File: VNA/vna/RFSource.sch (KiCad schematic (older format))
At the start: 15 parts, among them U4 AD9851, X1 30MHz

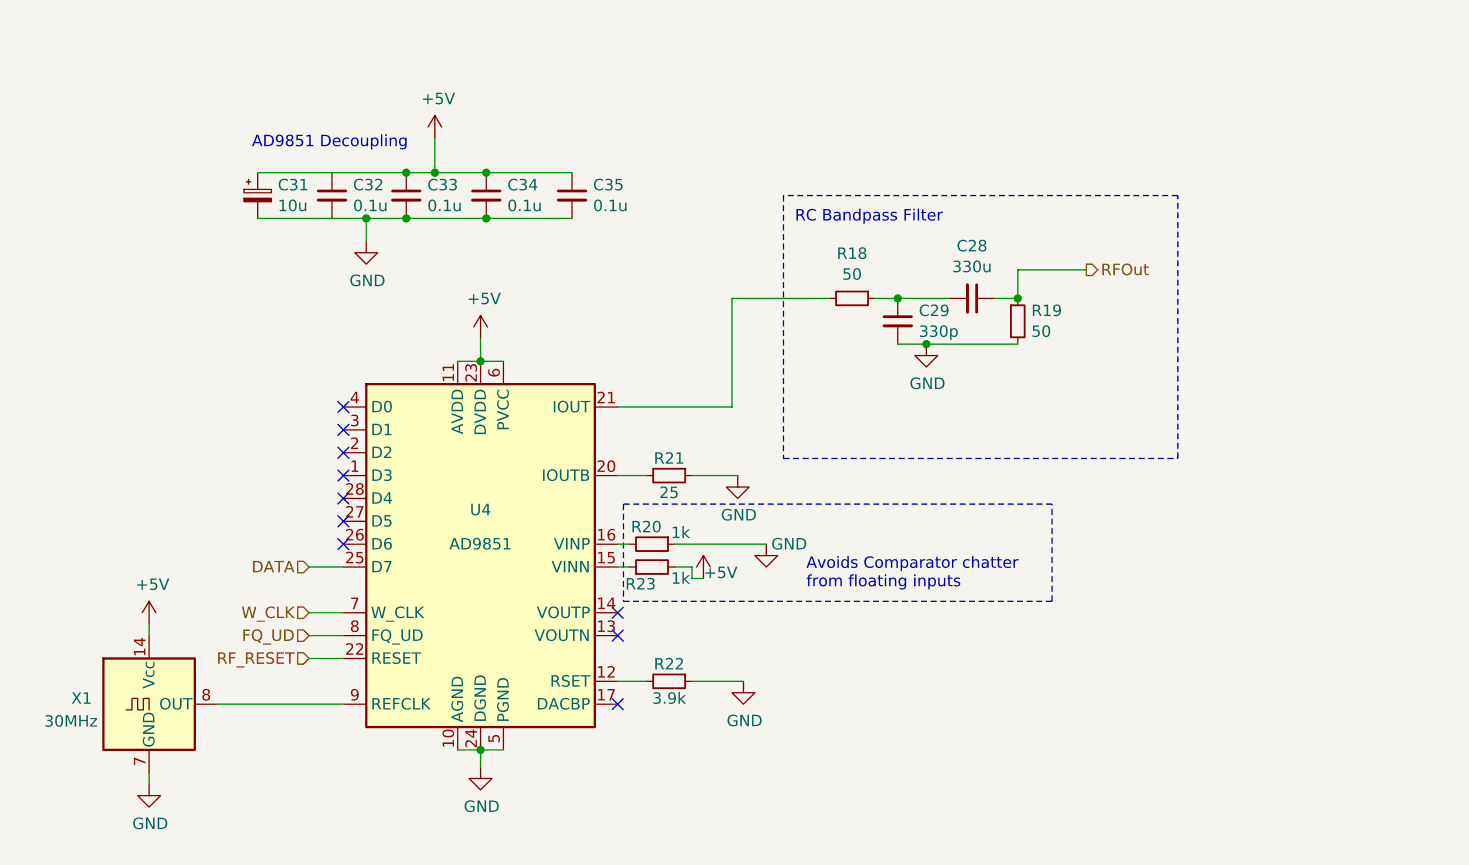
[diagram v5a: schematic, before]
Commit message: initial pcb design
initial layout and grouping of components complete
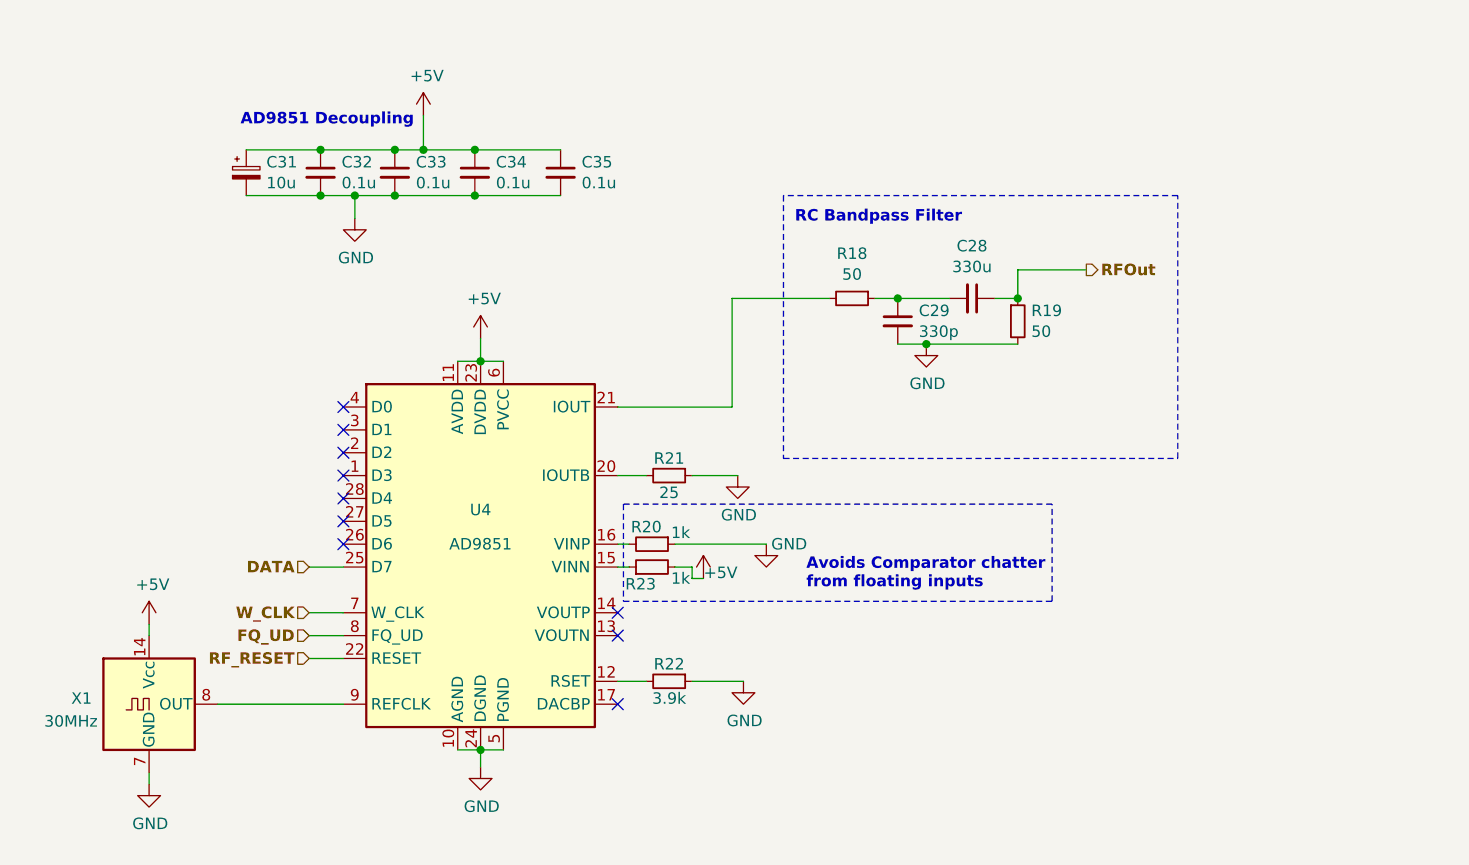
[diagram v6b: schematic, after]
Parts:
- C28, C29, C32, C33, C34, C35: footprint Capacitor_SMD:C_1206_3216Metric_Pad1.42x1.75mm_HandSolder -> Capacitor_SMD:C_0805_2012Metric_Pad1.15x1.40mm_HandSolder
- C31: footprint Capacitor_SMD:CP_Elec_6.3x5.4_Nichicon -> Capacitor_SMD:C_0805_2012Metric_Pad1.15x1.40mm_HandSolder
- R18, R19, R20, R21, R22, R23: footprint Resistor_SMD:R_1206_3216Metric_Pad1.42x1.75mm_HandSolder -> Resistor_SMD:R_0805_2012Metric_Pad1.15x1.40mm_HandSolder
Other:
- moved on the sheet: C31, C32, C33, C34, C35
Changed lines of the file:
@@
 encoding utf-8
 Sheet 9 10
-Title ""
-Date ""
-Rev ""
-Comp ""
+Title "RF Source"
+Date "2019-09-25"
+Rev "0.1"
+Comp "Benjamin Jackson"
 Comment1 ""
 Comment2 ""
@@
 Comment4 ""
 $EndDescr
-Text HLabel 6900 3400 2    50   Output ~ 0
+Text HLabel 6900 3400 2    50   Output ~ 10
 RFOut
-Text HLabel 3500 4900 0    50   Input ~ 0
+Text HLabel 3500 4900 0    50   Input ~ 10
 W_CLK
-Text HLabel 3500 5000 0    50   Input ~ 0
+Text HLabel 3500 5000 0    50   Input ~ 10
 FQ_UD
-Text HLabel 3500 4700 0    50   Input ~ 0
+Text HLabel 3500 4700 0    50   Input ~ 10
 DATA
-Text HLabel 3500 5100 0    50   Input ~ 0
+Text HLabel 3500 5100 0    50   Input ~ 10
 RF_RESET
 Connection ~ 4250 5500
@@
 F 0 "R22" V 5000 5200 50  0000 C CNN
 F 1 "3.9k" V 5150 5200 50  0000 C CNN
-F 2 "Resistor_SMD:R_1206_3216Metric_Pad1.42x1.75mm_HandSolder" H 5075 5200 50  0001 C CNN
+F 2 "Resistor_SMD:R_0805_2012Metric_Pad1.15x1.40mm_HandSolder" H 5075 5200 50  0001 C CNN
 F 3 "~" H 5075 5200 50  0001 C CNN
 	1    5075 5200
@@
 F 0 "R21" V 5000 4300 50  0000 C CNN
 F 1 "25" V 5150 4300 50  0000 C CNN
-F 2 "Resistor_SMD:R_1206_3216Metric_Pad1.42x1.75mm_HandSolder" H 5075 4300 50  0001 C CNN
+F 2 "Resistor_SMD:R_0805_2012Metric_Pad1.15x1.40mm_HandSolder" H 5075 4300 50  0001 C CNN
 F 3 "~" H 5075 4300 50  0001 C CNN
 	1    5075 4300
@@
 Wire Wire Line
 	5350 4000 5350 3525
-Text Notes 5625 3200 0    50   ~ 0
+Text Notes 5625 3200 0    50   ~ 10
 RC Bandpass Filter
 $Comp
@@
 F 0 "R18" V 5679 3525 50  0000 C CNN
 F 1 "50" V 5770 3525 50  0000 C CNN
-F 2 "Resistor_SMD:R_1206_3216Metric_Pad1.42x1.75mm_HandSolder" H 5875 3525 50  0001 C CNN
+F 2 "Resistor_SMD:R_0805_2012Metric_Pad1.15x1.40mm_HandSolder" H 5875 3525 50  0001 C CNN
 F 3 "~" H 5875 3525 50  0001 C CNN
 	1    5875 3525
@@
 F 0 "R19" H 6659 3671 50  0000 L CNN
 F 1 "50" H 6659 3580 50  0000 L CNN
-F 2 "Resistor_SMD:R_1206_3216Metric_Pad1.42x1.75mm_HandSolder" H 6600 3625 50  0001 C CNN
+F 2 "Resistor_SMD:R_0805_2012Metric_Pad1.15x1.40mm_HandSolder" H 6600 3625 50  0001 C CNN
 F 3 "~" H 6600 3625 50  0001 C CNN
 	1    6600 3625
@@
 F 0 "C29" H 6167 3671 50  0000 L CNN
 F 1 "330p" H 6167 3580 50  0000 L CNN
-F 2 "Capacitor_SMD:C_1206_3216Metric_Pad1.42x1.75mm_HandSolder" H 6075 3625 50  0001 C CNN
+F 2 "Capacitor_SMD:C_0805_2012Metric_Pad1.15x1.40mm_HandSolder" H 6075 3625 50  0001 C CNN
 F 3 "~" H 6075 3625 50  0001 C CNN
 	1    6075 3625
@@
 F 0 "C28" V 6171 3525 50  0000 C CNN
 F 1 "330u" V 6262 3525 50  0000 C CNN
-F 2 "Capacitor_SMD:C_1206_3216Metric_Pad1.42x1.75mm_HandSolder" H 6400 3525 50  0001 C CNN
+F 2 "Capacitor_SMD:C_0805_2012Metric_Pad1.15x1.40mm_HandSolder" H 6400 3525 50  0001 C CNN
 F 3 "~" H 6400 3525 50  0001 C CNN
 	1    6400 3525
@@
 F 0 "R20" V 4925 4575 50  0000 C CNN
 F 1 "1k" V 4950 4725 50  0000 C CNN
-F 2 "Resistor_SMD:R_1206_3216Metric_Pad1.42x1.75mm_HandSolder" H 5000 4600 50  0001 C CNN
+F 2 "Resistor_SMD:R_0805_2012Metric_Pad1.15x1.40mm_HandSolder" H 5000 4600 50  0001 C CNN
 F 3 "~" H 5000 4600 50  0001 C CNN
 	1    5000 4600
@@
 F 0 "R23" V 4925 4750 50  0000 C CNN
 F 1 "1k" V 4950 4575 50  0000 C CNN
-F 2 "Resistor_SMD:R_1206_3216Metric_Pad1.42x1.75mm_HandSolder" H 5000 4700 50  0001 C CNN
+F 2 "Resistor_SMD:R_0805_2012Metric_Pad1.15x1.40mm_HandSolder" H 5000 4700 50  0001 C CNN
 F 3 "~" H 5000 4700 50  0001 C CNN
 	1    5000 4700
@@
 L Device:C_Small C35
 U 1 1 5D95F03A
-P 4650 3075
-F 0 "C35" H 4742 3121 50  0000 L CNN
-F 1 "0.1u" H 4742 3030 50  0000 L CNN
-F 2 "Capacitor_SMD:C_1206_3216Metric_Pad1.42x1.75mm_HandSolder" H 4650 3075 50  0001 C CNN
-F 3 "~" H 4650 3075 50  0001 C CNN
-	1    4650 3075
+P 4600 2975
+F 0 "C35" H 4692 3021 50  0000 L CNN
+F 1 "0.1u" H 4692 2930 50  0000 L CNN
+F 2 "Capacitor_SMD:C_0805_2012Metric_Pad1.15x1.40mm_HandSolder" H 4600 2975 50  0001 C CNN
+F 3 "~" H 4600 2975 50  0001 C CNN
+	1    4600 2975
 	1    0    0    -1
 $EndComp
@@
 L Device:C_Small C34
 U 1 1 5D961801
-P 4275 3075
-F 0 "C34" H 4367 3121 50  0000 L CNN
-F 1 "0.1u" H 4367 3030 50  0000 L CNN
-F 2 "Capacitor_SMD:C_1206_3216Metric_Pad1.42x1.75mm_HandSolder" H 4275 3075 50  0001 C CNN
-F 3 "~" H 4275 3075 50  0001 C CNN
-	1    4275 3075
+P 4225 2975
+F 0 "C34" H 4317 3021 50  0000 L CNN
+F 1 "0.1u" H 4317 2930 50  0000 L CNN
+F 2 "Capacitor_SMD:C_0805_2012Metric_Pad1.15x1.40mm_HandSolder" H 4225 2975 50  0001 C CNN
+F 3 "~" H 4225 2975 50  0001 C CNN
+	1    4225 2975
 	1    0    0    -1
 $EndComp
@@
 L Device:C_Small C33
 U 1 1 5D961E48
-P 3925 3075
-F 0 "C33" H 4017 3121 50  0000 L CNN
-F 1 "0.1u" H 4017 3030 50  0000 L CNN
-F 2 "Capacitor_SMD:C_1206_3216Metric_Pad1.42x1.75mm_HandSolder" H 3925 3075 50  0001 C CNN
-F 3 "~" H 3925 3075 50  0001 C CNN
-	1    3925 3075
+P 3875 2975
+F 0 "C33" H 3967 3021 50  0000 L CNN
+F 1 "0.1u" H 3967 2930 50  0000 L CNN
+F 2 "Capacitor_SMD:C_0805_2012Metric_Pad1.15x1.40mm_HandSolder" H 3875 2975 50  0001 C CNN
+F 3 "~" H 3875 2975 50  0001 C CNN
+	1    3875 2975
 	1    0    0    -1
 $EndComp
@@
 L Device:C_Small C32
 U 1 1 5D9624FC
-P 3600 3075
-F 0 "C32" H 3692 3121 50  0000 L CNN
-F 1 "0.1u" H 3692 3030 50  0000 L CNN
-F 2 "Capacitor_SMD:C_1206_3216Metric_Pad1.42x1.75mm_HandSolder" H 3600 3075 50  0001 C CNN
-F 3 "~" H 3600 3075 50  0001 C CNN
-	1    3600 3075
-	1    0    0    -1
-$EndComp
-Wire Wire Line
-	3600 2975 3925 2975
-Wire Wire Line
-	3925 2975 4050 2975
-Connection ~ 3925 2975
-Wire Wire Line
-	4275 2975 4650 2975
-Connection ~ 4275 2975
-Wire Wire Line
-	3925 3175 4275 3175
-Wire Wire Line
-	4275 3175 4650 3175
-Connection ~ 4275 3175
-Wire Wire Line
-	3925 3175 3750 3175
-Connection ~ 3925 3175
+P 3550 2975
+F 0 "C32" H 3642 3021 50  0000 L CNN
+F 1 "0.1u" H 3642 2930 50  0000 L CNN
+F 2 "Capacitor_SMD:C_0805_2012Metric_Pad1.15x1.40mm_HandSolder" H 3550 2975 50  0001 C CNN
+F 3 "~" H 3550 2975 50  0001 C CNN
+	1    3550 2975
+	1    0    0    -1
+$EndComp
+Wire Wire Line
+	3550 2875 3875 2875
+Wire Wire Line
+	3875 2875 4000 2875
+Connection ~ 3875 2875
+Wire Wire Line
+	4225 2875 4600 2875
+Connection ~ 4225 2875
+Wire Wire Line
+	3875 3075 4225 3075
+Wire Wire Line
+	4225 3075 4600 3075
+Connection ~ 4225 3075
+Wire Wire Line
+	3875 3075 3700 3075
+Connection ~ 3875 3075
 $Comp
 L Device:CP_Small C31
 U 1 1 5D9681A5
-P 3275 3075
-F 0 "C31" H 3363 3121 50  0000 L CNN
-F 1 "10u" H 3363 3030 50  0000 L CNN
-F 2 "Capacitor_SMD:CP_Elec_6.3x5.4_Nichicon" H 3275 3075 50  0001 C CNN
-F 3 "~" H 3275 3075 50  0001 C CNN
-	1    3275 3075
-	1    0    0    -1
-$EndComp
-Wire Wire Line
-	3275 2975 3600 2975
-Wire Wire Line
-	3600 3175 3275 3175
+P 3225 2975
+F 0 "C31" H 3313 3021 50  0000 L CNN
+F 1 "10u" H 3313 2930 50  0000 L CNN
+F 2 "Capacitor_SMD:C_0805_2012Metric_Pad1.15x1.40mm_HandSolder" H 3225 2975 50  0001 C CNN
+F 3 "~" H 3225 2975 50  0001 C CNN
+	1    3225 2975
+	1    0    0    -1
+$EndComp
+Wire Wire Line
+	3225 2875 3550 2875
+Wire Wire Line
+	3550 3075 3225 3075
 $Comp
 L power:+5V #PWR0115
 U 1 1 5D968DE4
-P 4050 2825
-F 0 "#PWR0115" H 4050 2675 50  0001 C CNN
-F 1 "+5V" H 4065 2998 50  0000 C CNN
-F 2 "" H 4050 2825 50  0001 C CNN
-F 3 "" H 4050 2825 50  0001 C CNN
-	1    4050 2825
+P 4000 2725
+F 0 "#PWR0115" H 4000 2575 50  0001 C CNN
+F 1 "+5V" H 4015 2898 50  0000 C CNN
+F 2 "" H 4000 2725 50  0001 C CNN
+F 3 "" H 4000 2725 50  0001 C CNN
+	1    4000 2725
 	1    0    0    -1
 $EndComp
@@
 L power:GND #PWR0116
 U 1 1 5D969BB8
-P 3750 3275
-F 0 "#PWR0116" H 3750 3025 50  0001 C CNN
-F 1 "GND" H 3755 3102 50  0000 C CNN
-F 2 "" H 3750 3275 50  0001 C CNN
-F 3 "" H 3750 3275 50  0001 C CNN
-	1    3750 3275
-	1    0    0    -1
-$EndComp
-Wire Wire Line
-	3750 3275 3750 3175
-Connection ~ 3750 3175
-Wire Wire Line
-	3750 3175 3600 3175
-Wire Wire Line
-	4050 2825 4050 2975
-Connection ~ 4050 2975
-Wire Wire Line
-	4050 2975 4275 2975
+P 3700 3175
+F 0 "#PWR0116" H 3700 2925 50  0001 C CNN
+F 1 "GND" H 3705 3002 50  0000 C CNN
+F 2 "" H 3700 3175 50  0001 C CNN
+F 3 "" H 3700 3175 50  0001 C CNN
+	1    3700 3175
+	1    0    0    -1
+$EndComp
+Wire Wire Line
+	3700 3175 3700 3075
+Connection ~ 3700 3075
+Wire Wire Line
+	3700 3075 3550 3075
+Wire Wire Line
+	4000 2725 4000 2875
+Connection ~ 4000 2875
+Wire Wire Line
+	4000 2875 4225 2875
 Wire Notes Line
 	4875 4425 4875 4850
@@
 Wire Notes Line
 	6750 4425 4875 4425
-Text Notes 5675 4800 0    50   ~ 0
+Text Notes 5675 4800 0    50   ~ 10
 Avoids Comparator chatter \nfrom floating inputs
-Text Notes 3250 2875 0    50   ~ 0
+Text Notes 3200 2775 0    50   ~ 10
 AD9851 Decoupling
+Connection ~ 3550 2875
+Connection ~ 3550 3075
 $EndSCHEMATC

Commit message: v0.1 completed, producing gerbers
gerbers to be sent to jlc pcb pending their acceptance, they will be produced
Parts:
- added C13, C36, C37: 470p, Capacitor_SMD:C_0805_2012Metric_Pad1.15x1.40mm_HandSolder, symbol Device:C_Small
- added U10: BGA2851, Package_TO_SOT_SMD:SOT-363_SC-70-6, symbol RF_Amplifier:BGA2851
- C28: value 330u -> 100n
- C29: value 330p -> 1n
- R18: value 50 -> 16k
- R19: value 50 -> 100m
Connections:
- net +5V: now also C13.1, U10.1 (Vcc)
- net GND: now also R18.2, C13.2, U10.2 (G), U10.4 (G), U10.5 (G); no longer R19.2
- net RFOut: now also C37.1; no longer C28.1, R19.1
- net at U4.21 (IOUT): now also C28.2; no longer R18.2
- new net: C28.1, R18.1, R19.1
- new net: C29.1, C36.2, R19.2
- new net: C37.2, U10.3
- new net: C36.1, U10.6
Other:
- note added: "MMIC Amplifier\nmatched internally\nin/out to 50ohm"
- moved on the sheet: C28, C29, R18, R19
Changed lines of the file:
@@
 Comment4 ""
 $EndDescr
-Text HLabel 6900 3400 2    50   Output ~ 10
+Text HLabel 8150 3525 2    50   Output ~ 10
 RFOut
 Text HLabel 3500 4900 0    50   Input ~ 10
@@
 Wire Wire Line
 	5350 4000 5350 3525
-Text Notes 5625 3200 0    50   ~ 10
+Text Notes 5650 3225 0    50   ~ 10
 RC Bandpass Filter
 $Comp
 L power:GND #PWR0102
 U 1 1 5D858459
-P 6200 3725
-F 0 "#PWR0102" H 6200 3475 50  0001 C CNN
-F 1 "GND" H 6205 3552 50  0000 C CNN
-F 2 "" H 6200 3725 50  0001 C CNN
-F 3 "" H 6200 3725 50  0001 C CNN
-	1    6200 3725
+P 6200 3825
+F 0 "#PWR0102" H 6200 3575 50  0001 C CNN
+F 1 "GND" H 6205 3652 50  0000 C CNN
+F 2 "" H 6200 3825 50  0001 C CNN
+F 3 "" H 6200 3825 50  0001 C CNN
+	1    6200 3825
 	1    0    0    -1
 $EndComp
@@
 L Device:R_Small R18
 U 1 1 5D90E295
-P 5875 3525
-F 0 "R18" V 5679 3525 50  0000 C CNN
-F 1 "50" V 5770 3525 50  0000 C CNN
-F 2 "Resistor_SMD:R_0805_2012Metric_Pad1.15x1.40mm_HandSolder" H 5875 3525 50  0001 C CNN
-F 3 "~" H 5875 3525 50  0001 C CNN
-	1    5875 3525
-	0    1    1    0
+P 5950 3650
+F 0 "R18" V 6025 3650 50  0000 C CNN
+F 1 "16k" V 5875 3650 50  0000 C CNN
+F 2 "Resistor_SMD:R_0805_2012Metric_Pad1.15x1.40mm_HandSolder" H 5950 3650 50  0001 C CNN
+F 3 "~" H 5950 3650 50  0001 C CNN
+	1    5950 3650
+	1    0    0    -1
 $EndComp
 $Comp
 L Device:R_Small R19
 U 1 1 5D90EC5A
-P 6600 3625
-F 0 "R19" H 6659 3671 50  0000 L CNN
-F 1 "50" H 6659 3580 50  0000 L CNN
-F 2 "Resistor_SMD:R_0805_2012Metric_Pad1.15x1.40mm_HandSolder" H 6600 3625 50  0001 C CNN
-F 3 "~" H 6600 3625 50  0001 C CNN
-	1    6600 3625
-	1    0    0    -1
+P 6200 3525
+F 0 "R19" V 6350 3450 50  0000 L CNN
+F 1 "100m" V 6275 3425 50  0000 L CNN
+F 2 "Resistor_SMD:R_0805_2012Metric_Pad1.15x1.40mm_HandSolder" H 6200 3525 50  0001 C CNN
+F 3 "~" H 6200 3525 50  0001 C CNN
+	1    6200 3525
+	0    -1   -1   0
 $EndComp
 $Comp
 L Device:C_Small C29
 U 1 1 5D90F928
-P 6075 3625
-F 0 "C29" H 6167 3671 50  0000 L CNN
-F 1 "330p" H 6167 3580 50  0000 L CNN
-F 2 "Capacitor_SMD:C_0805_2012Metric_Pad1.15x1.40mm_HandSolder" H 6075 3625 50  0001 C CNN
-F 3 "~" H 6075 3625 50  0001 C CNN
-	1    6075 3625
+P 6400 3625
+F 0 "C29" H 6492 3671 50  0000 L CNN
+F 1 "1n" H 6492 3580 50  0000 L CNN
+F 2 "Capacitor_SMD:C_0805_2012Metric_Pad1.15x1.40mm_HandSolder" H 6400 3625 50  0001 C CNN
+F 3 "~" H 6400 3625 50  0001 C CNN
+	1    6400 3625
 	1    0    0    -1
 $EndComp
@@
 L Device:C_Small C28
 U 1 1 5D9103E4
-P 6400 3525
-F 0 "C28" V 6171 3525 50  0000 C CNN
-F 1 "330u" V 6262 3525 50  0000 C CNN
-F 2 "Capacitor_SMD:C_0805_2012Metric_Pad1.15x1.40mm_HandSolder" H 6400 3525 50  0001 C CNN
-F 3 "~" H 6400 3525 50  0001 C CNN
-	1    6400 3525
+P 5750 3525
+F 0 "C28" V 5521 3525 50  0000 C CNN
+F 1 "100n" V 5612 3525 50  0000 C CNN
+F 2 "Capacitor_SMD:C_0805_2012Metric_Pad1.15x1.40mm_HandSolder" H 5750 3525 50  0001 C CNN
+F 3 "~" H 5750 3525 50  0001 C CNN
+	1    5750 3525
 	0    1    1    0
 $EndComp
-Wire Wire Line
-	5350 3525 5775 3525
-Wire Wire Line
-	5975 3525 6075 3525
-Wire Wire Line
-	6075 3525 6300 3525
-Connection ~ 6075 3525
-Wire Wire Line
-	6500 3525 6600 3525
-Wire Wire Line
-	6075 3725 6200 3725
-Connection ~ 6200 3725
-Wire Wire Line
-	6200 3725 6600 3725
-Wire Wire Line
-	6600 3525 6600 3400
-Wire Wire Line
-	6600 3400 6900 3400
-Connection ~ 6600 3525
-Wire Notes Line
-	5575 3075 5575 4225
-Wire Notes Line
-	5575 4225 7300 4225
-Wire Notes Line
-	7300 4225 7300 3075
-Wire Notes Line
-	7300 3075 5575 3075
 $Comp
 L Device:R_Small R20
@@
 Connection ~ 3550 2875
 Connection ~ 3550 3075
+$Comp
+L RF_Amplifier:BGA2851 U10
+U 1 1 5D98BDCA
+P 7475 3525
+F 0 "U10" H 7500 3650 50  0000 L CNN
+F 1 "BGA2851" H 7475 3375 50  0000 L CNN
+F 2 "Package_TO_SOT_SMD:SOT-363_SC-70-6" H 7425 2875 50  0001 C CNN
+F 3 "https://www.nxp.com/docs/en/data-sheet/BGA2851.pdf" H 7475 3525 50  0001 C CNN
+	1    7475 3525
+	1    0    0    -1
+$EndComp
+$Comp
+L power:+5V #PWR0120
+U 1 1 5D98ED21
+P 7375 3175
+F 0 "#PWR0120" H 7375 3025 50  0001 C CNN
+F 1 "+5V" H 7390 3348 50  0000 C CNN
+F 2 "" H 7375 3175 50  0001 C CNN
+F 3 "" H 7375 3175 50  0001 C CNN
+	1    7375 3175
+	1    0    0    -1
+$EndComp
+$Comp
+L power:GND #PWR0121
+U 1 1 5D98FE3B
+P 7375 3875
+F 0 "#PWR0121" H 7375 3625 50  0001 C CNN
+F 1 "GND" H 7380 3702 50  0000 C CNN
+F 2 "" H 7375 3875 50  0001 C CNN
+F 3 "" H 7375 3875 50  0001 C CNN
+	1    7375 3875
+	1    0    0    -1
+$EndComp
+Text Notes 6950 2675 0    50   ~ 10
+MMIC Amplifier\nmatched internally\nin/out to 50ohm
+Wire Wire Line
+	5350 3525 5650 3525
+Wire Wire Line
+	5850 3525 5950 3525
+Wire Wire Line
+	5950 3550 5950 3525
+Connection ~ 5950 3525
+Wire Wire Line
+	5950 3525 6100 3525
+Wire Wire Line
+	6300 3525 6400 3525
+Wire Wire Line
+	5950 3750 6200 3750
+Wire Wire Line
+	6400 3750 6400 3725
+Wire Wire Line
+	6200 3750 6200 3825
+Connection ~ 6200 3750
+Wire Wire Line
+	6200 3750 6400 3750
+Wire Notes Line
+	5625 3125 5625 4050
+Wire Notes Line
+	5625 4050 6725 4050
+Wire Notes Line
+	6725 4050 6725 3125
+Wire Notes Line
+	6725 3125 5625 3125
+Wire Wire Line
+	7375 3825 7375 3875
+Wire Wire Line
+	7375 3225 7375 3175
+$Comp
+L Device:C_Small C37
+U 1 1 5D9C2425
+P 7950 3525
+F 0 "C37" V 7721 3525 50  0000 C CNN
+F 1 "470p" V 7812 3525 50  0000 C CNN
+F 2 "Capacitor_SMD:C_0805_2012Metric_Pad1.15x1.40mm_HandSolder" H 7950 3525 50  0001 C CNN
+F 3 "~" H 7950 3525 50  0001 C CNN
+	1    7950 3525
+	0    1    1    0
+$EndComp
+$Comp
+L Device:C_Small C36
+U 1 1 5D9C3B15
+P 7025 3525
+F 0 "C36" V 6796 3525 50  0000 C CNN
+F 1 "470p" V 6887 3525 50  0000 C CNN
+F 2 "Capacitor_SMD:C_0805_2012Metric_Pad1.15x1.40mm_HandSolder" H 7025 3525 50  0001 C CNN
+F 3 "~" H 7025 3525 50  0001 C CNN
+	1    7025 3525
+	0    1    1    0
+$EndComp
+$Comp
+L Device:C_Small C13
+U 1 1 5D9C4738
+P 7725 2875
+F 0 "C13" H 7817 2921 50  0000 L CNN
+F 1 "470p" H 7817 2830 50  0000 L CNN
+F 2 "Capacitor_SMD:C_0805_2012Metric_Pad1.15x1.40mm_HandSolder" H 7725 2875 50  0001 C CNN
+F 3 "~" H 7725 2875 50  0001 C CNN
+	1    7725 2875
+	1    0    0    -1
+$EndComp
+Wire Wire Line
+	7125 3525 7175 3525
+Wire Wire Line
+	7775 3525 7850 3525
+Wire Wire Line
+	8050 3525 8150 3525
+Wire Notes Line
+	6925 4125 8075 4125
+Wire Notes Line
+	8075 4125 8075 2375
+Wire Notes Line
+	8075 2375 6925 2375
+Wire Notes Line
+	6925 2375 6925 4125
+Wire Wire Line
+	6400 3525 6925 3525
+Connection ~ 6400 3525
+$Comp
+L power:GND #PWR0122
+U 1 1 5D9DDA37
+P 7725 2975
+F 0 "#PWR0122" H 7725 2725 50  0001 C CNN
+F 1 "GND" H 7730 2802 50  0000 C CNN
+F 2 "" H 7725 2975 50  0001 C CNN
+F 3 "" H 7725 2975 50  0001 C CNN
+	1    7725 2975
+	1    0    0    -1
+$EndComp
+$Comp
+L power:+5V #PWR0123
+U 1 1 5D9DE892
+P 7725 2775
+F 0 "#PWR0123" H 7725 2625 50  0001 C CNN
+F 1 "+5V" H 7740 2948 50  0000 C CNN
+F 2 "" H 7725 2775 50  0001 C CNN
+F 3 "" H 7725 2775 50  0001 C CNN
+	1    7725 2775
+	1    0    0    -1
+$EndComp
 $EndSCHEMATC
